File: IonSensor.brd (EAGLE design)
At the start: 50.8 x 22.9 mm, 44 parts, among them IC1 QUAD_OPAMPD, IC2 QUAD_OPAMPD, IC3 QUAD_OPAMPD, X1 B4B-XH-2

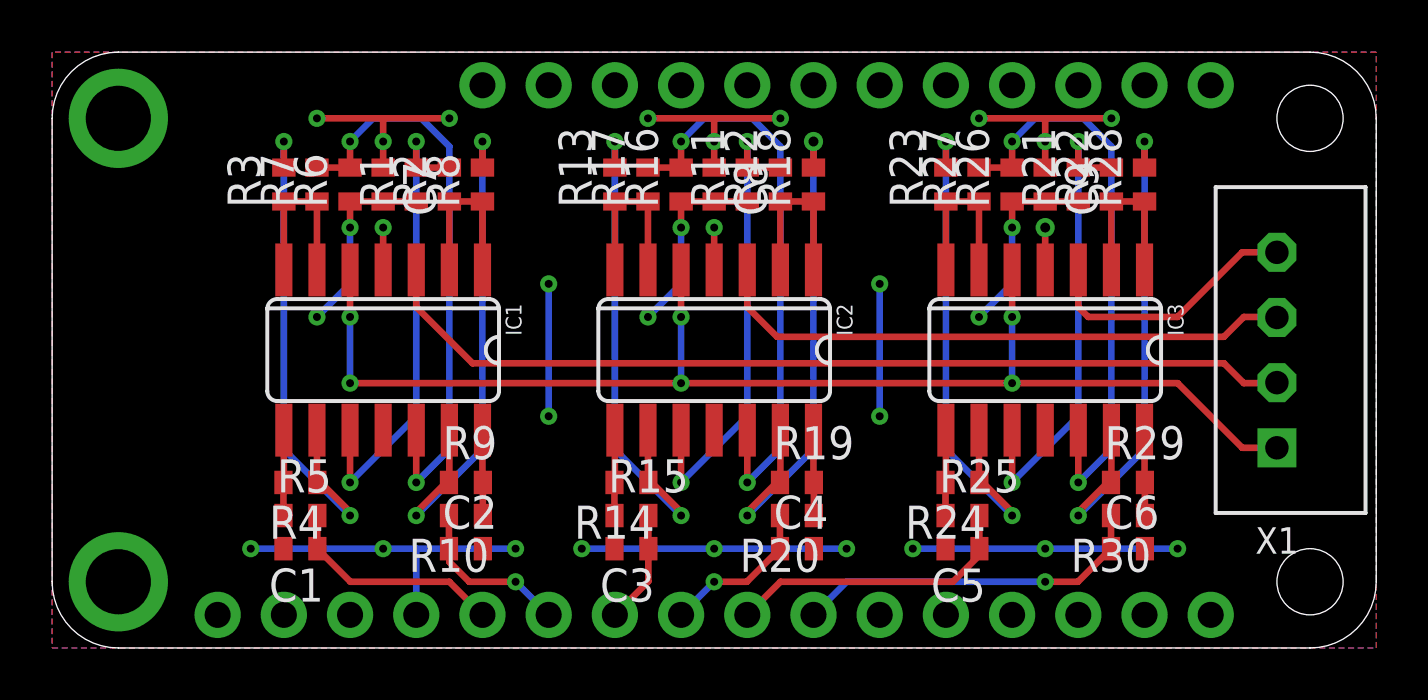
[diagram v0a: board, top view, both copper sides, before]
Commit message: Revert "Routing complete"
This reverts commit f47511b647111c71903cb3d4dec75a0fe3392e94.
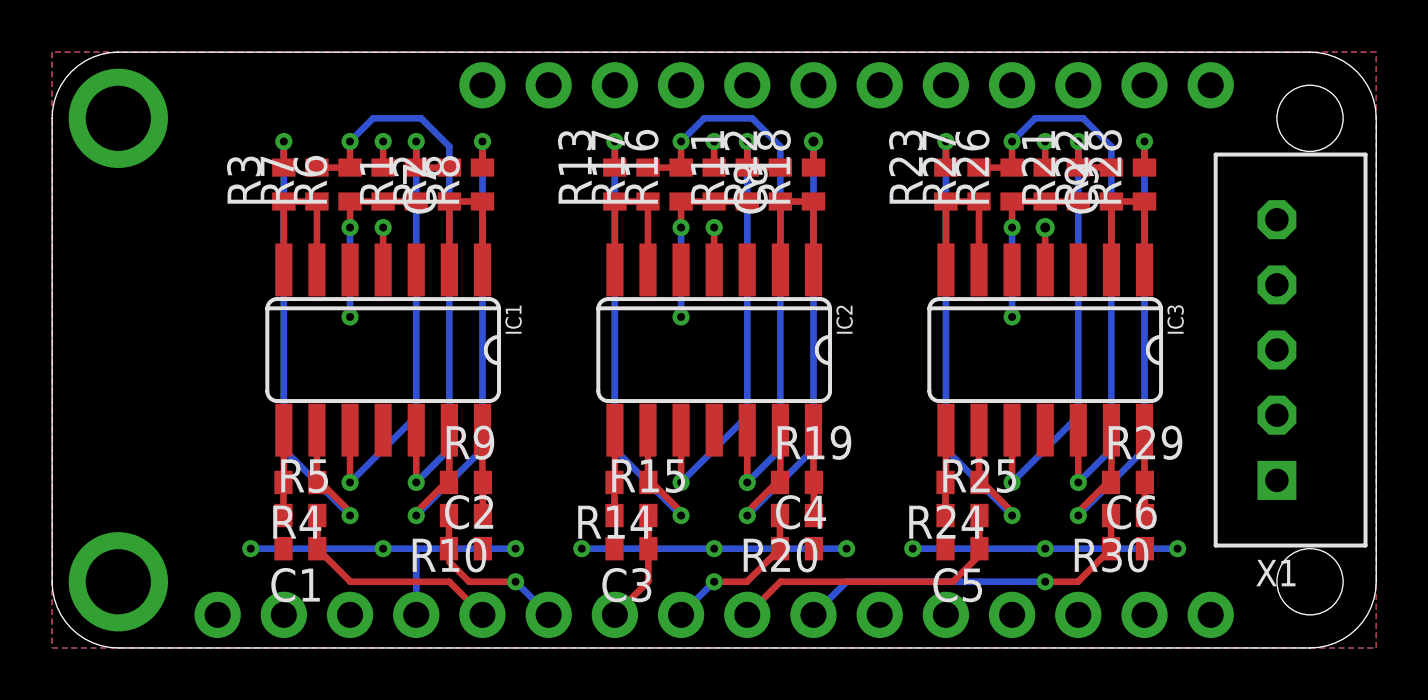
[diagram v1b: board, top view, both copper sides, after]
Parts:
- X1: value B4B-XH-2 -> B5B-XH-2; device con-JST XH:B4B-XH-A -> con-JST XH:B5B-XH-A
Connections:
- net CH0: now also X1.4; no longer X1.2
- net CH2: now also X1.2; no longer X1.4
- net GND: now also X1.1
- net REF: now also X1.5; no longer X1.1
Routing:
- net REF: track 49.6 -> 0.00 mm, vias 6 -> 0
- net CH0: track 35.7 -> 0.00 mm
- net CH1: track 22.5 -> 0.00 mm
- net +3V3: track 25.8 -> 7.88 mm, vias 12 -> 6
- net GND: track 65.7 -> 53.9 mm, vias 19 -> 15
- net CH2: track 10.2 -> 0.00 mm
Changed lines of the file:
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@@
 <attribute name="VALUE" x="36.068" y="18.669" size="1.27" layer="27" rot="R270"/>
 </element>
-<element name="X1" library="con-JST XH" package="B4B-XH-A" value="B4B-XH-2" x="46.99" y="11.43" smashed="yes" rot="R270">
-<attribute name="NAME" x="46.99" y="4.632" size="1.016" layer="25" rot="R180" align="bottom-center"/>
-<attribute name="VALUE" x="48.26" y="7.68" size="1.016" layer="27" rot="R270" align="bottom-right"/>
+<element name="X1" library="con-JST XH" package="B5B-XH-A" value="B5B-XH-2" x="46.99" y="11.43" smashed="yes" rot="R270">
+<attribute name="NAME" x="46.99" y="3.382" size="1.016" layer="25" rot="R180" align="bottom-center"/>
+<attribute name="VALUE" x="48.26" y="6.43" size="1.016" layer="27" rot="R270" align="bottom-right"/>
 </element>
 </elements>
@@
 <wire x1="36.83" y1="17.13" x2="38.1" y2="17.13" width="0.254" layer="1"/>
 <wire x1="38.1" y1="17.13" x2="39.37" y2="17.13" width="0.254" layer="1"/>
-<via x="10.16" y="12.7" extent="1-16" drill="0.3048"/>
-<via x="22.86" y="12.7" extent="1-16" drill="0.3048"/>
-<via x="35.56" y="12.7" extent="1-16" drill="0.3048"/>
-<wire x1="11.43" y1="16.129" x2="11.43" y2="13.97" width="0.254" layer="16"/>
-<wire x1="11.43" y1="13.97" x2="10.16" y2="12.7" width="0.254" layer="16"/>
-<wire x1="24.13" y1="16.129" x2="24.13" y2="13.97" width="0.254" layer="16"/>
-<wire x1="24.13" y1="13.97" x2="22.86" y2="12.7" width="0.254" layer="16"/>
-<wire x1="36.83" y1="16.129" x2="36.83" y2="13.97" width="0.254" layer="16"/>
-<wire x1="36.83" y1="13.97" x2="35.56" y2="12.7" width="0.254" layer="16"/>
-<via x="19.05" y="8.89" extent="1-16" drill="0.3048"/>
-<via x="19.05" y="13.97" extent="1-16" drill="0.3048"/>
-<via x="31.75" y="8.89" extent="1-16" drill="0.3048"/>
-<via x="31.75" y="13.97" extent="1-16" drill="0.3048"/>
-<wire x1="19.05" y1="13.97" x2="19.05" y2="8.89" width="0.254" layer="16"/>
-<wire x1="31.75" y1="13.97" x2="31.75" y2="8.89" width="0.254" layer="16"/>
+<via x="11.43" y="12.7" extent="1-16" drill="0.3048"/>
+<via x="24.13" y="12.7" extent="1-16" drill="0.3048"/>
+<via x="36.83" y="12.7" extent="1-16" drill="0.3048"/>
+<wire x1="11.43" y1="16.129" x2="11.43" y2="12.7" width="0.254" layer="16"/>
+<wire x1="24.13" y1="16.129" x2="24.13" y2="12.7" width="0.254" layer="16"/>
+<wire x1="36.83" y1="16.129" x2="36.83" y2="12.7" width="0.254" layer="16"/>
+<contactref element="X1" pad="1"/>
+<wire x1="38.1" y1="8.3566" x2="36.83" y2="12.7" width="0" layer="19" extent="1-1"/>
+<wire x1="38.1" y1="3.81" x2="38.1" y2="8.3566" width="0" layer="19" extent="1-1"/>
+<wire x1="41.925" y1="3.81" x2="43.18" y2="3.81" width="0" layer="19" extent="1-1"/>
+<wire x1="34.275" y1="3.81" x2="33.02" y2="3.81" width="0" layer="19" extent="1-1"/>
+<wire x1="30.48" y1="3.81" x2="33.02" y2="3.81" width="0" layer="19" extent="1-1"/>
+<wire x1="29.225" y1="3.81" x2="30.48" y2="3.81" width="0" layer="19" extent="1-1"/>
+<wire x1="21.575" y1="3.81" x2="20.32" y2="3.81" width="0" layer="19" extent="1-1"/>
+<wire x1="17.78" y1="3.81" x2="20.32" y2="3.81" width="0" layer="19" extent="1-1"/>
+<wire x1="16.525" y1="3.81" x2="17.78" y2="3.81" width="0" layer="19" extent="1-1"/>
+<wire x1="8.875" y1="3.81" x2="7.62" y2="3.81" width="0" layer="19" extent="1-1"/>
+<wire x1="25.4" y1="8.3566" x2="25.4" y2="3.81" width="0" layer="19" extent="1-1"/>
+<wire x1="24.13" y1="12.7" x2="25.4" y2="8.3566" width="0" layer="19" extent="1-1"/>
+<wire x1="12.7" y1="8.3566" x2="12.7" y2="3.81" width="0" layer="19" extent="1-1"/>
+<wire x1="11.43" y1="12.7" x2="12.7" y2="8.3566" width="0" layer="19" extent="1-1"/>
+<wire x1="46.99" y1="6.43" x2="7.62" y2="3.81" width="0" layer="19" extent="1-1"/>
 </signal>
 <signal name="+3V3">
@@
 <wire x1="25.4" y1="18.43" x2="25.4" y2="19.431" width="0.254" layer="1"/>
 <wire x1="38.1" y1="18.43" x2="38.1" y2="19.431" width="0.254" layer="1"/>
-<via x="10.16" y="20.32" extent="1-16" drill="0.3048"/>
-<wire x1="10.16" y1="20.32" x2="12.7" y2="20.32" width="0.254" layer="1"/>
-<via x="15.24" y="20.32" extent="1-16" drill="0.3048"/>
-<via x="22.86" y="20.32" extent="1-16" drill="0.3048"/>
-<via x="27.94" y="20.32" extent="1-16" drill="0.3048"/>
-<via x="35.56" y="20.32" extent="1-16" drill="0.3048"/>
-<via x="40.64" y="20.32" extent="1-16" drill="0.3048"/>
-<wire x1="12.7" y1="20.32" x2="15.24" y2="20.32" width="0.254" layer="1"/>
-<wire x1="22.86" y1="20.32" x2="25.4" y2="20.32" width="0.254" layer="1"/>
-<wire x1="25.4" y1="20.32" x2="27.94" y2="20.32" width="0.254" layer="1"/>
-<wire x1="35.56" y1="20.32" x2="38.1" y2="20.32" width="0.254" layer="1"/>
-<wire x1="38.1" y1="20.32" x2="40.64" y2="20.32" width="0.254" layer="1"/>
-<wire x1="12.7" y1="19.431" x2="12.7" y2="20.32" width="0.254" layer="1"/>
-<wire x1="25.4" y1="19.431" x2="25.4" y2="20.32" width="0.254" layer="1"/>
-<wire x1="38.1" y1="19.431" x2="38.1" y2="20.32" width="0.254" layer="1"/>
+<wire x1="25.4" y1="16.129" x2="38.1" y2="16.129" width="0" layer="19" extent="1-1"/>
 </signal>
 <signal name="CH0">
 <contactref element="IC1" pad="3"/>
-<contactref element="X1" pad="2"/>
-<wire x1="13.97" y1="14.5034" x2="13.97" y2="13.081" width="0.254" layer="1"/>
-<wire x1="13.97" y1="13.081" x2="16.129" y2="10.922" width="0.254" layer="1"/>
-<wire x1="44.958" y1="10.922" x2="45.72" y2="10.16" width="0.254" layer="1"/>
-<wire x1="45.72" y1="10.16" x2="46.97" y2="10.16" width="0.254" layer="1"/>
-<wire x1="46.97" y1="10.16" x2="46.99" y2="10.18" width="0.254" layer="1"/>
-<wire x1="16.129" y1="10.922" x2="44.958" y2="10.922" width="0.254" layer="1"/>
+<contactref element="X1" pad="4"/>
+<wire x1="46.99" y1="13.93" x2="13.97" y2="14.5034" width="0" layer="19" extent="1-1"/>
 </signal>
 <signal name="CH1">
 <contactref element="IC2" pad="3"/>
 <contactref element="X1" pad="3"/>
-<wire x1="26.67" y1="14.5034" x2="26.67" y2="13.081" width="0.254" layer="1"/>
-<wire x1="26.67" y1="13.081" x2="27.813" y2="11.938" width="0.254" layer="1"/>
-<wire x1="27.813" y1="11.938" x2="44.958" y2="11.938" width="0.254" layer="1"/>
-<wire x1="44.958" y1="11.938" x2="45.72" y2="12.7" width="0.254" layer="1"/>
-<wire x1="45.72" y1="12.7" x2="46.97" y2="12.7" width="0.254" layer="1"/>
-<wire x1="46.97" y1="12.7" x2="46.99" y2="12.68" width="0.254" layer="1"/>
+<wire x1="46.99" y1="11.43" x2="26.67" y2="14.5034" width="0" layer="19" extent="1-1"/>
 </signal>
 <signal name="CH2">
 <contactref element="IC3" pad="3"/>
-<contactref element="X1" pad="4"/>
-<wire x1="39.751" y1="12.7" x2="39.37" y2="13.081" width="0.254" layer="1"/>
-<wire x1="39.37" y1="14.5034" x2="39.37" y2="13.081" width="0.254" layer="1"/>
-<wire x1="39.751" y1="12.7" x2="43.18" y2="12.7" width="0.254" layer="1"/>
-<wire x1="46.99" y1="15.18" x2="45.66" y2="15.18" width="0.254" layer="1"/>
-<wire x1="45.66" y1="15.18" x2="43.18" y2="12.7" width="0.254" layer="1"/>
+<contactref element="X1" pad="2"/>
+<wire x1="46.99" y1="8.93" x2="39.37" y2="14.5034" width="0" layer="19" extent="1-1"/>
 </signal>
 <signal name="REF">
@@
 <contactref element="IC2" pad="5"/>
 <contactref element="IC3" pad="5"/>
-<wire x1="11.43" y1="14.5034" x2="11.43" y2="12.7" width="0.254" layer="1"/>
-<via x="11.43" y="12.7" extent="1-16" drill="0.3048"/>
-<wire x1="11.43" y1="12.7" x2="11.43" y2="10.16" width="0.254" layer="16"/>
-<via x="11.43" y="10.16" extent="1-16" drill="0.3048"/>
-<wire x1="24.13" y1="14.5034" x2="24.13" y2="12.7" width="0.254" layer="1"/>
-<via x="24.13" y="12.7" extent="1-16" drill="0.3048"/>
-<wire x1="24.13" y1="12.7" x2="24.13" y2="10.16" width="0.254" layer="16"/>
-<via x="24.13" y="10.16" extent="1-16" drill="0.3048"/>
-<wire x1="36.83" y1="14.5034" x2="36.83" y2="12.7" width="0.254" layer="1"/>
-<via x="36.83" y="12.7" extent="1-16" drill="0.3048"/>
-<wire x1="36.83" y1="12.7" x2="36.83" y2="10.16" width="0.254" layer="16"/>
-<via x="36.83" y="10.16" extent="1-16" drill="0.3048"/>
-<contactref element="X1" pad="1"/>
-<wire x1="11.43" y1="10.16" x2="24.13" y2="10.16" width="0.254" layer="1"/>
-<wire x1="24.13" y1="10.16" x2="36.83" y2="10.16" width="0.254" layer="1"/>
-<wire x1="36.83" y1="10.16" x2="43.18" y2="10.16" width="0.254" layer="1"/>
-<wire x1="46.99" y1="7.68" x2="45.66" y2="7.68" width="0.254" layer="1"/>
-<wire x1="45.66" y1="7.68" x2="43.18" y2="10.16" width="0.254" layer="1"/>
+<contactref element="X1" pad="5"/>
+<wire x1="24.13" y1="14.5034" x2="36.83" y2="14.5034" width="0" layer="19" extent="1-1"/>
+<wire x1="11.43" y1="14.5034" x2="24.13" y2="14.5034" width="0" layer="19" extent="1-1"/>
+<wire x1="46.99" y1="16.43" x2="11.43" y2="14.5034" width="0" layer="19" extent="1-1"/>
 </signal>
 <signal name="C1+">
